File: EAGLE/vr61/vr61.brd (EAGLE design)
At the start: 283 x 93 mm, 235 parts, among them J6 MICROMOD-2222-C

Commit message: i think it's ready
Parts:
- moved D35 6.32 mm to (143.0, 44.1)
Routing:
- net N$35: track 50.3 -> 47.0 mm, vias 0 -> 2
- net MY2: track 249.5 -> 248.6 mm
- net MX6: track 397.4 -> 398.0 mm
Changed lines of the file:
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@@
 <attribute name="NAME" x="115.154" y="45.3" size="1" layer="26" rot="MR0"/>
 </element>
-<element name="D35" library="jlcpcb_basic_parts" package="SOD-123" value="" x="137.8" y="40.525" smashed="yes" rot="MR0">
-<attribute name="NAME" x="139.454" y="41.7" size="1" layer="26" rot="MR0"/>
+<element name="D35" library="jlcpcb_basic_parts" package="SOD-123" value="" x="143" y="44.125" smashed="yes" rot="MR0">
+<attribute name="NAME" x="144.654" y="45.3" size="1" layer="26" rot="MR0"/>
 </element>
 <element name="D36" library="jlcpcb_basic_parts" package="SOD-123" value="" x="151.5" y="44.125" smashed="yes" rot="MR0">
@@
 <contactref element="D35" pad="A"/>
 <contactref element="S_H" pad="P$3"/>
-<wire x1="136.1617" y1="40.525" x2="136.1617" y2="41.6617" width="0.254" layer="16"/>
-<wire x1="145.5" y1="43" x2="146" y2="43.5" width="0.254" layer="16"/>
-<wire x1="146" y1="43.5" x2="146" y2="54.15" width="0.254" layer="16"/>
-<wire x1="146" y1="54.15" x2="138.8" y2="61.35" width="0.254" layer="16"/>
+<wire x1="138.8" y1="61.35" x2="146" y2="54.15" width="0.254" layer="16"/>
 <wire x1="130.665" y1="58.365" x2="130.665" y2="50.04" width="0.254" layer="16"/>
-<wire x1="136.1617" y1="41.6617" x2="137.5" y2="43" width="0.254" layer="16"/>
-<wire x1="137.5" y1="43" x2="145.5" y2="43" width="0.254" layer="16"/>
 <wire x1="138.8" y1="61.35" x2="133.65" y2="61.35" width="0.254" layer="16"/>
 <wire x1="133.65" y1="61.35" x2="130.665" y2="58.365" width="0.254" layer="16"/>
+<wire x1="146" y1="50.5" x2="145.7" y2="50.2" width="0.254" layer="16"/>
+<via x="145.7" y="50.2" extent="1-16" drill="0.35"/>
+<wire x1="145.7" y1="50.2" x2="146" y2="49.9" width="0.254" layer="1"/>
+<wire x1="146" y1="49.9" x2="146" y2="45" width="0.254" layer="1"/>
+<wire x1="146" y1="45" x2="143.458" y2="42.458" width="0.254" layer="1"/>
+<wire x1="143.458" y1="42.458" x2="140.8" y2="42.458" width="0.254" layer="1"/>
+<wire x1="140.8" y1="42.458" x2="139.9" y2="43.358" width="0.254" layer="1"/>
+<wire x1="139.9" y1="43.358" x2="139.9" y2="44.1" width="0.254" layer="1"/>
+<via x="139.9" y="44.1" extent="1-16" drill="0.35"/>
+<wire x1="139.9" y1="44.1" x2="141.3367" y2="44.1" width="0.254" layer="16"/>
+<wire x1="141.3367" y1="44.1" x2="141.3617" y2="44.125" width="0.254" layer="16"/>
+<wire x1="146" y1="54.15" x2="146" y2="50.5" width="0.254" layer="16"/>
 <wire x1="130.665" y1="50.04" x2="133.94" y2="50.04" width="0" layer="19" extent="16-16"/>
 </signal>
@@
 <contactref element="S_H" pad="P$4"/>
 <contactref element="S_J" pad="P$4"/>
-<wire x1="140.29" y1="52.58" x2="147.2" y2="52.58" width="0.254" layer="1"/>
-<wire x1="147.2" y1="52.58" x2="151" y2="52.58" width="0.254" layer="1"/>
+<wire x1="140.29" y1="52.58" x2="146.6" y2="52.58" width="0.254" layer="1"/>
+<wire x1="146.6" y1="52.58" x2="151" y2="52.58" width="0.254" layer="1"/>
 <wire x1="154.95" y1="52.58" x2="159.29" y2="52.58" width="0.254" layer="1"/>
 <wire x1="121" y1="52.58" x2="121.29" y2="52.58" width="0.254" layer="1"/>
@@
 <wire x1="109.5" y1="57" x2="109.5" y2="46.75" width="0.254" layer="1"/>
 <wire x1="109.5" y1="46.75" x2="114.3" y2="41.95" width="0.254" layer="1"/>
-<wire x1="147.2" y1="44.25" x2="147.2" y2="52.58" width="0.254" layer="1"/>
-<wire x1="114.3" y1="41.95" x2="144.9" y2="41.95" width="0.254" layer="1"/>
-<wire x1="144.9" y1="41.95" x2="147.2" y2="44.25" width="0.254" layer="1"/>
+<wire x1="146.6" y1="44.85" x2="146.6" y2="52.58" width="0.254" layer="1"/>
+<wire x1="114.3" y1="41.95" x2="143.7" y2="41.95" width="0.254" layer="1"/>
+<wire x1="143.7" y1="41.95" x2="146.6" y2="44.85" width="0.254" layer="1"/>
 <wire x1="151" y1="52.58" x2="151.52" y2="53.1" width="0.254" layer="1"/>
 <wire x1="154.43" y1="53.1" x2="154.95" y2="52.58" width="0.254" layer="1"/>
@@
 <via x="85" y="66.5" extent="1-16" drill="0.35"/>
 <via x="76.4" y="54.9" extent="1-16" drill="0.35"/>
-<via x="138.5" y="37" extent="1-16" drill="0.35"/>
+<via x="138.4" y="38" extent="1-16" drill="0.35"/>
 <via x="105.5" y="43" extent="1-16" drill="0.35"/>
 <via x="65" y="45" extent="1-16" drill="0.35"/>
@@
 <via x="49.5" y="77" extent="1-16" drill="0.35"/>
 <via x="146" y="35.5" extent="1-16" drill="0.35"/>
-<via x="148.5" y="39.5" extent="1-16" drill="0.35"/>
+<via x="148.6" y="39.4" extent="1-16" drill="0.35"/>
 <via x="107.5" y="49.5" extent="1-16" drill="0.35"/>
 <wire x1="19.9" y1="77.9" x2="17.4" y2="77.9" width="0.254" layer="16"/>
@@
 <wire x1="137.575" y1="63.375" x2="129.1383" y2="63.375" width="0.254" layer="16"/>
 <wire x1="146.55" y1="54.4" x2="137.575" y2="63.375" width="0.254" layer="16"/>
-<wire x1="146.55" y1="54.4" x2="146.549996875" y2="43.299996875" width="0.254" layer="16"/>
-<wire x1="146.549996875" y1="43.299996875" x2="143.775" y2="40.525" width="0.254" layer="16"/>
-<wire x1="143.775" y1="40.525" x2="142" y2="40.525" width="0.254" layer="16"/>
-<wire x1="142" y1="40.525" x2="139.4383" y2="40.525" width="0.254" layer="16"/>
+<wire x1="146.55" y1="54.4" x2="146.549996875" y2="44.1" width="0.254" layer="16"/>
+<wire x1="146.549996875" y1="43.299996875" x2="146.549996875" y2="44.1" width="0.254" layer="16"/>
 <wire x1="73.45" y1="55.725" x2="73.45" y2="53.65" width="0.254" layer="16"/>
 <wire x1="73.45" y1="53.65" x2="73.5" y2="53.6" width="0.254" layer="16"/>
@@
 <wire x1="124.7633" y1="24.5" x2="135.5" y2="24.5" width="0.254" layer="16"/>
 <wire x1="135.5" y1="24.5" x2="137.2" y2="26.2" width="0.254" layer="16"/>
-<wire x1="137.2" y1="37.4" x2="139.5" y2="39.7" width="0.254" layer="16"/>
-<wire x1="139.5" y1="39.7" x2="139.5" y2="40.4633" width="0.254" layer="16"/>
-<wire x1="139.5" y1="40.4633" x2="139.4383" y2="40.525" width="0.254" layer="16"/>
-<wire x1="137.2" y1="26.2" x2="137.2" y2="37.4" width="0.254" layer="16"/>
+<wire x1="137.2" y1="26.2" x2="137.2" y2="33.95" width="0.254" layer="16"/>
 <via x="262.35" y="44.25" extent="1-16" drill="0.35"/>
 <wire x1="262.35" y1="44.25" x2="240.25" y2="44.25" width="0.254" layer="1"/>
@@
 <wire x1="260.2383" y1="19.2383" x2="260.2383" y2="17.95" width="0.254" layer="16"/>
 <wire x1="261.125" y1="20.125" x2="260.2383" y2="19.2383" width="0.254" layer="16"/>
+<wire x1="137.2" y1="33.95" x2="142.875" y2="39.625" width="0.254" layer="16"/>
+<wire x1="142.875" y1="39.625" x2="146.549996875" y2="43.299996875" width="0.254" layer="16"/>
+<wire x1="142" y1="40.525" x2="142.875" y2="39.65" width="0.254" layer="16"/>
+<wire x1="142.875" y1="39.65" x2="142.875" y2="39.625" width="0.254" layer="16"/>
+<wire x1="144.6383" y1="44.125" x2="146.524996875" y2="44.125" width="0.254" layer="16"/>
+<wire x1="146.524996875" y1="44.125" x2="146.549996875" y2="44.1" width="0.254" layer="16"/>
 </signal>
 <signal name="MX7">

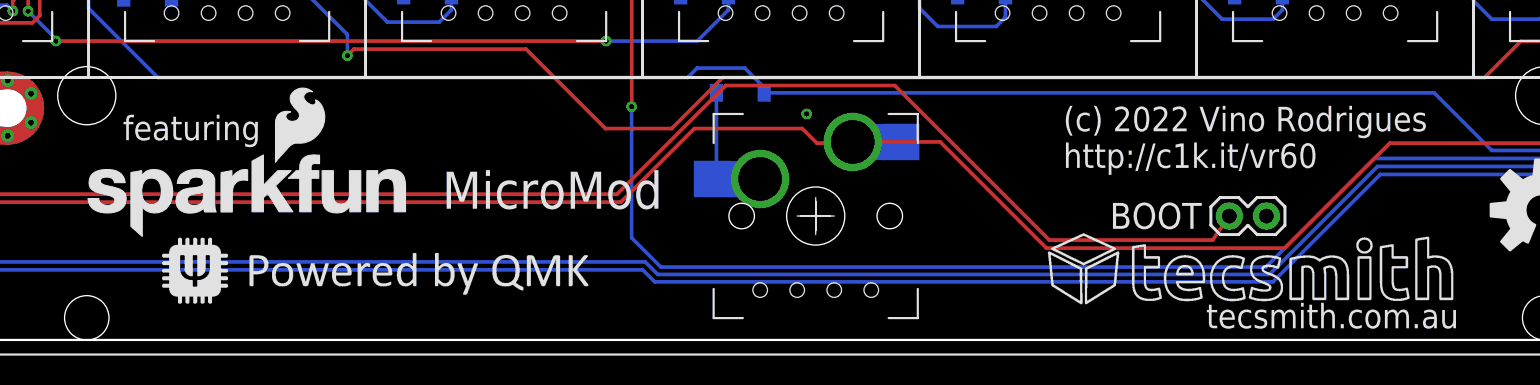
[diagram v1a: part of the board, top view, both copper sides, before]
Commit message: correct micromod logo
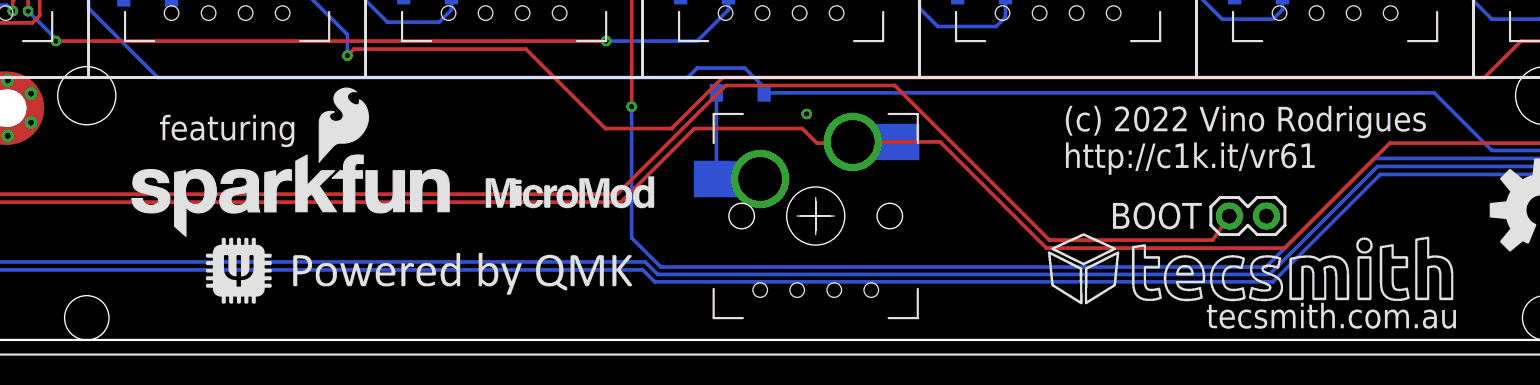
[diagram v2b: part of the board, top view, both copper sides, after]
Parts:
- added U$13, U$3: MICROMOD-LOGO, random_logos:MICROMOD-LOGO
- moved U$5 3.00 mm to (83.0, 8.00)
- moved U$6 3.00 mm to (88.7, 3.40)
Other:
- board text added: "(c) 2022 Vino Rodrigues http://c1k.it/vr61"
- board text removed: "(c) 2022 Vino Rodrigues http://c1k.it/vr60"
- board text removed: "MicroMod"
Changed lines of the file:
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@@
 <drawing>
 <settings>
-<setting alwaysvectorfont="yes"/>
+<setting alwaysvectorfont="no"/>
 <setting verticaltext="up"/>
 </settings>
@@
 <vertex x="34.6" y="23.4"/>
 <vertex x="36.5" y="21.5"/>
-<vertex x="36.5" y="18.4"/>
-<vertex x="43.2" y="18.4"/>
+<vertex x="36.5" y="18.8"/>
+<vertex x="43.2" y="18.8"/>
 <vertex x="43.2" y="26.2"/>
 </polygon>
@@
 <vertex x="34.55" y="23.45"/>
 <vertex x="36.5" y="21.5"/>
-<vertex x="36.5" y="18.4"/>
-<vertex x="43.2" y="18.4"/>
+<vertex x="36.5" y="18.8"/>
+<vertex x="43.2" y="18.8"/>
 <vertex x="43.2" y="26.2"/>
 </polygon>
@@
 <wire x1="191.8" y1="11.45" x2="189.2" y2="11.45" width="0.254" layer="22"/>
 <wire x1="191.8" y1="7.7" x2="189.2" y2="7.7" width="0.254" layer="22"/>
-<text x="105" y="10" size="2.54" layer="21" font="vector">MicroMod</text>
 <text x="157.4" y="1.8" size="1.6764" layer="21" font="vector">tecsmith.com.au</text>
 <text x="147.6" y="12.8" size="1.6764" layer="21" font="vector">(c) 2022 Vino Rodrigues
-http://c1k.it/vr60</text>
+http://c1k.it/vr61</text>
 <text x="157.1" y="10.4" size="1.778" layer="21" rot="R180">BOOT</text>
-<text x="83.1" y="14.7" size="1.6764" layer="21" font="vector">featuring</text>
+<text x="85.6" y="14.7" size="1.6764" layer="21" font="vector">featuring</text>
 <text x="117.1" y="14.7" size="1.6764" layer="22" font="vector" rot="MR0">featuring</text>
-<text x="95" y="10" size="2.54" layer="22" font="vector" rot="MR0">MicroMod</text>
 <text x="282.5" y="86" size="1.4224" layer="22" rot="MR90" align="top-center">JLCJLCJLCJLC</text>
 <text x="174.6" y="12.8" size="1.6764" layer="22" font="vector" rot="MR0">(c) 2022 Vino Rodrigues
-http://c1k.it/vr60</text>
+http://c1k.it/vr61</text>
 <text x="163.5" y="1.9" size="1.6764" layer="22" font="vector" rot="MR0">tecsmith.com.au</text>
 <text x="16.7" y="77.1" size="1.27" layer="26" rot="MR0">PTC</text>
@@
 <element name="SG4" library="ts_keyboards" package="MOUNTING-HOLE-VWIDE-C" value="MOUNTING-HOLE-VWIDEEDGE-CUT" x="282.5" y="38.3" smashed="yes" rot="R180"/>
 <element name="LOGO1" library="random_logos" package="OSHW-LOGO-L" value="OSHW-LOGOL" x="180.4" y="9.9" smashed="yes"/>
-<element name="U$5" library="random_logos" package="SFE_LOGO_NAME_FLAME_.2" value="SPARKFUN_LOGO0.2" x="80" y="8" smashed="yes"/>
-<element name="U$6" library="random_logos" package="QMK_LOGO" value="QMK_LOGO" x="85.7" y="3.4" smashed="yes"/>
+<element name="U$5" library="random_logos" package="SFE_LOGO_NAME_FLAME_.2" value="SPARKFUN_LOGO0.2" x="83" y="8" smashed="yes"/>
+<element name="U$6" library="random_logos" package="QMK_LOGO" value="QMK_LOGO" x="88.7" y="3.4" smashed="yes"/>
 <element name="U$8" library="random_logos" package="TECSMITH-NAME" value="TECSMITH-LOGOLONG" x="149" y="6" smashed="yes"/>
 <element name="U$10" library="random_logos" package="SFE_LOGO_NAME_FLAME_.2" value="SPARKFUN_LOGO0.2" x="120" y="8" smashed="yes" rot="MR0"/>
@@
 <element name="U$7" library="random_logos" package="TECSMITH-NAME" value="TECSMITH-LOGOLONG" x="172" y="6" smashed="yes" rot="MR0"/>
 <element name="LOGO2" library="random_logos" package="OSHW-LOGO-L" value="OSHW-LOGOL" x="180.4" y="9.9" smashed="yes" rot="MR0"/>
+<element name="U$3" library="random_logos" package="MICROMOD-LOGO" value="MICROMOD-LOGO" x="108" y="10" smashed="yes"/>
+<element name="U$13" library="random_logos" package="MICROMOD-LOGO" value="MICROMOD-LOGO" x="95" y="10" smashed="yes" rot="MR0"/>
 </elements>
 <signals>

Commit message: updates after peer review on qmk discord
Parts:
- removed D62: 1N4148, adafruit:SOD-123
- added D0: (no value), jlcpcb_basic_parts:SOD-123
- R1, R2: value 1.5k -> 5.1K; device SparkFun-Resistors:0603 -> rcl:R0603
- R3: value 150k -> 150K; device SparkFun-Resistors:0603 -> rcl:R0603
- R4: device SparkFun-Resistors:0603 -> rcl:R0603
- moved R3 6.87 mm to (35.6, 58.5), turned to 270 degrees
- moved R2 3.29 mm to (30.0, 91.0), turned to 90 degrees
- moved R4 1.68 mm to (40.4, 58.5), turned to 270 degrees
- moved R1 1.00 mm to (27.0, 91.0), turned to 270 degrees
- renumbered U1 to LM1117
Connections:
- net VCC: now also D0.A; no longer D62.A
- net VSUP: now also D0.C; no longer D62.C
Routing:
- net N$69: track 13.8 -> 22.5 mm
- net N$68: track 13.6 -> 5.70 mm
- net VIN/3: track 44.0 -> 49.1 mm
- net VCC: track 118.5 -> 122.7 mm
- net VSUP: track 413.1 -> 412.2 mm
- net N$67: track 11.5 -> 12.2 mm

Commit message: Update vr61.brd
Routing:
- net VBUS: track 30.5 -> 29.6 mm
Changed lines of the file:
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@@
 <setting verticaltext="up"/>
 </settings>
-<grid distance="1" unitdist="mm" unit="mm" style="dots" multiple="5" display="yes" altdistance="0.1" altunitdist="mm" altunit="mm"/>
+<grid distance="0.5" unitdist="mm" unit="mm" style="dots" multiple="5" display="yes" altdistance="0.05" altunitdist="mm" altunit="mm"/>
 <layers>
 <layer number="1" name="Top" color="4" fill="1" visible="yes" active="yes"/>
@@
 <contactref element="PTC" pad="P$1"/>
 <contactref element="ESD" pad="P$5"/>
-<wire x1="15.8" y1="88.545" x2="15.8" y2="87.2" width="0.508" layer="16"/>
-<wire x1="19" y1="84" x2="19" y2="81.5" width="0.508" layer="16"/>
-<wire x1="19" y1="81.5" x2="18" y2="80.5" width="0.508" layer="16"/>
+<wire x1="15.8" y1="88.545" x2="15.8" y2="87.6" width="0.508" layer="16"/>
+<wire x1="18.95" y1="84.7" x2="18.95" y2="81.45" width="0.508" layer="16"/>
+<wire x1="18.95" y1="81.45" x2="18" y2="80.5" width="0.508" layer="16"/>
 <wire x1="18" y1="80.5" x2="18" y2="79.5" width="0.508" layer="16"/>
-<wire x1="15.8" y1="87.2" x2="19" y2="84" width="0.508" layer="16"/>
-<wire x1="20.6" y1="88.545" x2="20.6" y2="87.4" width="0.508" layer="16"/>
-<wire x1="20.6" y1="87.4" x2="21" y2="87" width="0.508" layer="16"/>
-<wire x1="21" y1="87" x2="21" y2="86" width="0.508" layer="16"/>
-<wire x1="21" y1="86" x2="19" y2="84" width="0.508" layer="16"/>
+<wire x1="15.8" y1="87.6" x2="16.35" y2="87.05" width="0.508" layer="16"/>
+<wire x1="16.6" y1="87.05" x2="18.95" y2="84.7" width="0.508" layer="16"/>
 <wire x1="26.25" y1="75" x2="27.5" y2="75" width="0.508" layer="16"/>
 <via x="27.5" y="75" extent="1-16" drill="0.35"/>
@@
 <wire x1="20" y1="79.5" x2="18" y2="79.5" width="0.508" layer="16"/>
 <wire x1="27.5" y1="75" x2="22" y2="75" width="0.508" layer="1"/>
+<wire x1="16.35" y1="87.05" x2="16.6" y2="87.05" width="0.508" layer="16"/>
+<wire x1="20.6" y1="86.35" x2="18.95" y2="84.7" width="0.508" layer="16"/>
+<wire x1="20.6" y1="88.545" x2="20.6" y2="86.35" width="0.508" layer="16"/>
 </signal>
 <signal name="LED">

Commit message: added LED caps
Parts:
- added C10, C11, C7, C8, C9: 100nF, rcl:C0603
- moved J4 19.0 mm to (190.0, 91.0)
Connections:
- net GND: now also C10.2, C11.2, C7.2, C8.2, C9.2
- net VSUP: now also C10.1, C11.1, C7.1, C8.1, C9.1
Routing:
- net VSUP: track 412.2 -> 456.9 mm, vias 9 -> 11
- net N$72: track 8.00 -> 27.0 mm
- net N$62: track 15.7 -> 18.2 mm

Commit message: turned top row around
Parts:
- added R6: 220, rcl:R0603
- moved D10 17.1 mm to (171.0, 83.0)
- moved D6 17.1 mm to (95.0, 83.0)
- moved D7 17.1 mm to (114.0, 83.0)
- moved D8 17.1 mm to (133.0, 83.0)
- moved D9 17.1 mm to (152.0, 83.0)
- moved J4 13.5 mm to (190.0, 77.5), turned to 90 degrees
- moved C8 12.4 mm to (114.0, 77.5)
- moved C11 12.4 mm to (171.0, 77.5)
- moved C9 12.4 mm to (133.0, 77.5)
- moved C10 12.4 mm to (152.0, 77.5)
- moved LED-5 10.2 mm to (104.5, 80.4)
- moved LED-6 10.2 mm to (123.5, 80.4)
- moved LED-7 10.2 mm to (142.5, 80.4)
- moved LED-8 10.2 mm to (161.5, 80.4)
- moved D14 10.0 mm to (262.0, 76.0)
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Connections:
- new net LED1ST: L/SFT.2, R6.1
- net LED: now also R6.2; no longer L/SFT.2
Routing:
- net LED: track 72.0 -> 21.9 mm, vias 4 -> 2
- net LED1ST: track 0.00 -> 49.0 mm, vias 0 -> 2
- net VSUP: track 456.9 -> 412.4 mm
- net MX6: track 398.0 -> 411.5 mm, vias 6 -> 8
- net MY5: track 199.1 -> 212.1 mm
- net MY0: track 179.3 -> 188.1 mm, vias 2 -> 1
- net MX4: track 354.7 -> 346.5 mm, vias 7 -> 6
- net MX5: track 346.7 -> 339.7 mm, vias 9 -> 11
- net N$14: track 7.09 -> 13.4 mm
- net N$13: track 6.88 -> 13.0 mm
- net N$12: track 6.88 -> 13.0 mm
- net N$29: track 128.1 -> 122.7 mm
- net N$11: track 6.88 -> 12.2 mm
- net MX2: track 386.1 -> 381.3 mm
- net N$28: track 16.7 -> 21.1 mm
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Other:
- board text removed: "JLCJLCJLCJLC"

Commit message: production ready
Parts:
- removed L/SFT: MC74VHC1G50, ts_keyboards:SC-74A
- added JP2: G-OPT, SparkFun-Jumpers:SMT-JUMPER_2_NO_NO-SILK
- added Y1: 74AHCT1G125, ts_keyboards:SOT-23-5
- C1, C4: value 0.1uF -> 100nF
- C2, C5: value 0.22uF -> 22uF
- C3: value 1nF -> 4.7uF
- D0: value (none) -> B5819W SL
- J2: value (none) -> SM04B-SRSS-TB(LF)(SN)
- LM1117: value (none) -> AMS1117-3.3
- PTC: value PTC_ASMD1206 -> PTC_ASMD1206-150
- X1: value (none) -> TYPE-C-31-M-12
- renumbered S-EQL to S_EQL
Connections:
- net N$67 renamed CC1
- net N$69 renamed CC2
- removed net N$71: C6.1, R5.2, X1.M1, X1.M2, X1.M3, X1.M4
- new net GROUND: C6.1, JP2.1, R5.2, X1.M1, X1.M2, X1.M3, X1.M4
- net GND: now also Y1.1, Y1.3; no longer L/SFT.3
- net LED1ST: now also Y1.2; no longer L/SFT.2
- net N$70: now also Y1.4; no longer L/SFT.4
- net SC1: now also JP2.2
- net VSUP: now also Y1.5; no longer L/SFT.5
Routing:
- net GROUND: track 0.00 -> 61.6 mm, vias 0 -> 3
- net N$71: track 15.6 -> 0.00 mm
- net SC1: track 0.00 -> 13.3 mm, vias 0 -> 1
- net LED1ST: track 49.0 -> 49.8 mm
- net N$29: track 122.7 -> 122.0 mm
- net GND: vias 50 -> 52
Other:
- board text added: "GROUND"
- board text added: "JLCJLCJLCJLC"

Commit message: production ready, rev B
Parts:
- X1: device ts_keyboards:USB_C_CUSB31-CFM2AX-01-X -> ts_keyboards:TYPE-C-31-M-12
- moved TVS 18.8 mm to (16.0, 76.0)
- moved R1 17.8 mm to (12.8, 80.2)
- moved R2 16.8 mm to (14.5, 84.5)
- moved R5 15.5 mm to (26.5, 91.5), turned to 0 degrees
- moved C6 15.5 mm to (26.5, 89.5), turned to 180 degrees
- moved ESD 10.3 mm to (16.0, 80.0), turned to 180 degrees
- moved X1 4.60 mm to (18.2, 91.3)
- moved PTC 2.44 mm to (19.4, 80.0)
- moved D1 2.00 mm to (8.00, 74.0)
- moved S_ESC 1.00 mm to (10.5, 85.5), turned to 90 degrees
- moved D2 0.68 mm to (34.6, 89.5)
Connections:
- net CC1: now also X1.A5-CC1; no longer X1.A5
- net CC2: now also X1.B5-CC2; no longer X1.B5
- net D+: now also X1.A6-DP1, X1.B6-DP2; no longer X1.A6, X1.B6
- net D-: now also X1.A7-DN1, X1.B7-DN2; no longer X1.A7, X1.B7
- net GND: now also X1.A1B12-GND, X1.B1A12-GND; no longer X1.A1B12, X1.B1A12
- net VBUS: now also X1.A4B9-VBUS, X1.B4A9-VBUS; no longer X1.A4B9, X1.B4A9
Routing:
- net CC2: track 22.5 -> 8.80 mm
- net D+: track 91.6 -> 101.4 mm, vias 4 -> 6
- net D-: track 88.5 -> 98.1 mm
- net VBUS: track 29.6 -> 21.8 mm, vias 2 -> 4
- net GND: track 9.27 -> 2.12 mm, vias 52 -> 47
- net N$1: track 17.7 -> 10.8 mm
- net MY0: track 188.1 -> 193.6 mm
- net CC1: track 12.2 -> 9.34 mm, vias 0 -> 2
- net MX0: track 334.9 -> 336.5 mm
- net MX1: track 437.2 -> 438.4 mm
- net GROUND: track 61.6 -> 60.8 mm
